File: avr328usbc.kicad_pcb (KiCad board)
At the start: 2 copper layers, 21 parts, among them J1 USB_C_Receptacle, J2 Conn_02x05_Counter_Clockwise, J3 USB_C_Receptacle_PowerOnly_6P, J4 Conn_02x16_Counter_Clockwise, J5 AVR-ISP-6, U1 MCP2221AxP, U2 ACPL-772L-000E, U3 ACPL-772L-000E, U4 ATmega328P-P

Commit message: finished converting schematic to correct USBC and pin headers
Symbols didn't match the footprints
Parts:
- J1: value USB_C_Receptacle -> USB-C THT
- J2: value Conn_02x05_Counter_Clockwise -> MCP Debug Header
- J3: value USB_C_Receptacle_PowerOnly_6P -> USB-C THT
- J4: value Conn_02x16_Counter_Clockwise -> AVR Pin Header
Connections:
- J2 pad 10: GND_USB -> /MCP.SDA
- J2 pad 2: /MCP.GP0 -> GND_USB
- J2 pad 3: /MCP.GP1 -> /MCP.GP0
- J2 pad 4: /MCP.GP2 -> /MCP.UTx
- J2 pad 5: /MCP.GP3 -> /MCP.GP1
- J2 pad 6: /MCP.SDA -> /MCP.URx
- J2 pad 7: /MCP.SCL -> /MCP.GP2
- J2 pad 8: /MCP.URx -> /MCP.SCL
- J2 pad 9: /MCP.UTx -> /MCP.GP3
- J3 pad A1: (no net) -> GND_AVR
- J3 pad A4: (no net) -> VCC_AVR
- J3 pad A6: (no net) -> unconnected-(J3-D+-PadA6)
- J3 pad A7: (no net) -> unconnected-(J3-D--PadA7)
- J3 pad A8: (no net) -> unconnected-(J3-SBU1-PadA8)
- J3 pad B1: (no net) -> GND_AVR
- J3 pad B4: (no net) -> VCC_AVR
- J3 pad B6: (no net) -> unconnected-(J3-D+-PadB6)
- J3 pad B7: (no net) -> unconnected-(J3-D--PadB7)
- J3 pad B8: (no net) -> unconnected-(J3-SBU2-PadB8)
- J4 pad 10: /MCU Sheet/PC1 -> /MCU Sheet/PD4
- J4 pad 11: /MCU Sheet/PC2 -> /MCU Sheet/PB5
- J4 pad 12: /MCU Sheet/PC3 -> /MCU Sheet/PD5
- J4 pad 13: /MCU Sheet/PC4 -> /MCU Sheet/PB6
- J4 pad 14: /MCU Sheet/PC5 -> /MCU Sheet/PD6
- J4 pad 15: /MCU Sheet/PC6 #RESET -> /MCU Sheet/PB7
- J4 pad 16: GND_AVR -> /MCU Sheet/PD7
- J4 pad 17: VCC_AVR -> /MCU Sheet/PC0
- J4 pad 18: unconnected-(J4-Pin_18-Pad18) -> GND_AVR
- J4 pad 19: unconnected-(J4-Pin_19-Pad19) -> /MCU Sheet/PC1
- J4 pad 2: /MCU Sheet/PB1 -> /UART_Rx
- J4 pad 21: unconnected-(J4-Pin_21-Pad21) -> /MCU Sheet/PC2
- J4 pad 23: unconnected-(J4-Pin_23-Pad23) -> /MCU Sheet/PC3
- J4 pad 24: GND_AVR -> unconnected-(J4-Pin_24-Pad24)
- J4 pad 25: /MCU Sheet/PD7 -> /MCU Sheet/PC4
- J4 pad 26: /MCU Sheet/PD6 -> unconnected-(J4-Pin_26-Pad26)
- J4 pad 27: /MCU Sheet/PD5 -> /MCU Sheet/PC5
- J4 pad 28: /MCU Sheet/PD4 -> unconnected-(J4-Pin_28-Pad28)
- J4 pad 29: /MCU Sheet/PD3 -> /MCU Sheet/PC6 #RESET
- J4 pad 3: /MCU Sheet/PB2 -> /MCU Sheet/PB1
- J4 pad 30: /MCU Sheet/PD2 -> unconnected-(J4-Pin_30-Pad30)
- J4 pad 31: /UART_Tx -> GND_AVR
- J4 pad 32: /UART_Rx -> VCC_AVR
- J4 pad 4: /MCU Sheet/PB3 -> /UART_Tx
- J4 pad 5: /MCU Sheet/PB4 -> /MCU Sheet/PB2
- J4 pad 6: /MCU Sheet/PB5 -> /MCU Sheet/PD2
- J4 pad 7: /MCU Sheet/PB6 -> /MCU Sheet/PB3
- J4 pad 8: /MCU Sheet/PB7 -> /MCU Sheet/PD3
- J4 pad 9: /MCU Sheet/PC0 -> /MCU Sheet/PB4

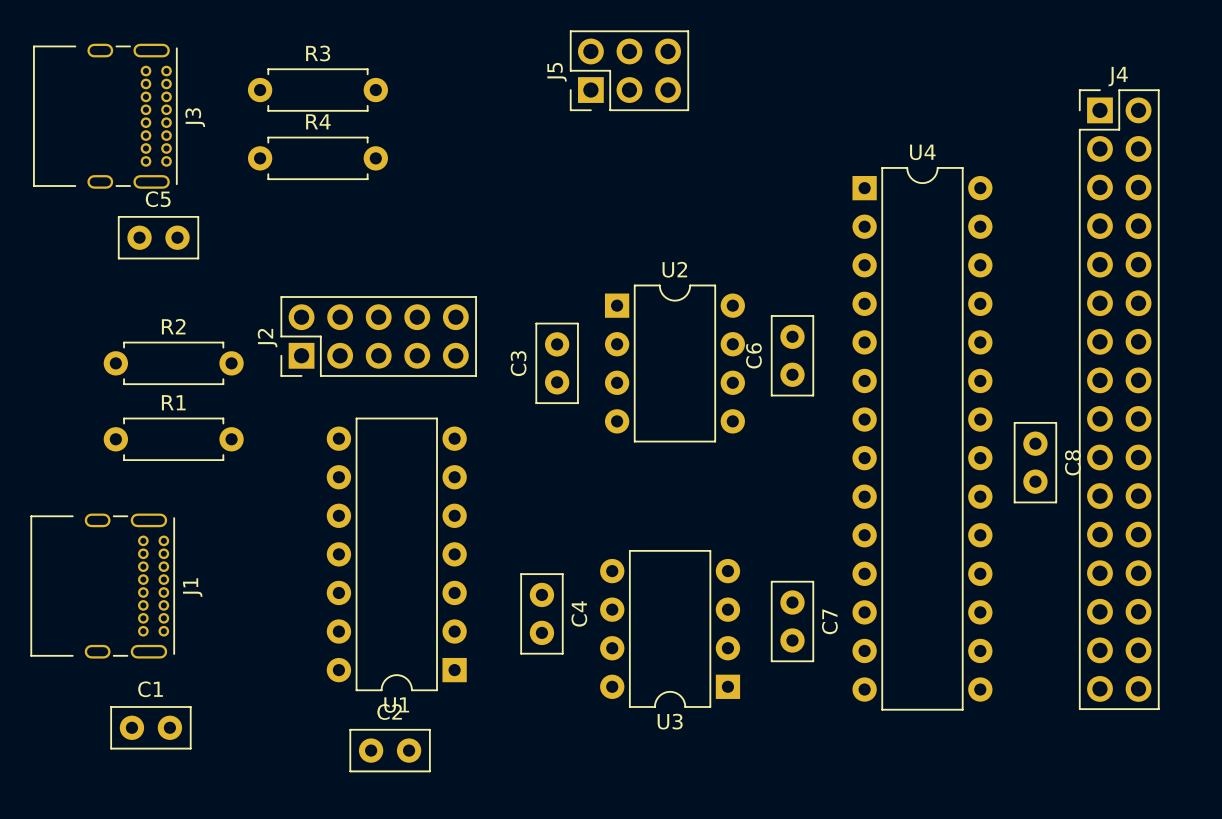
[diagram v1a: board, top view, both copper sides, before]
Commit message: pcb footprints placed and locked
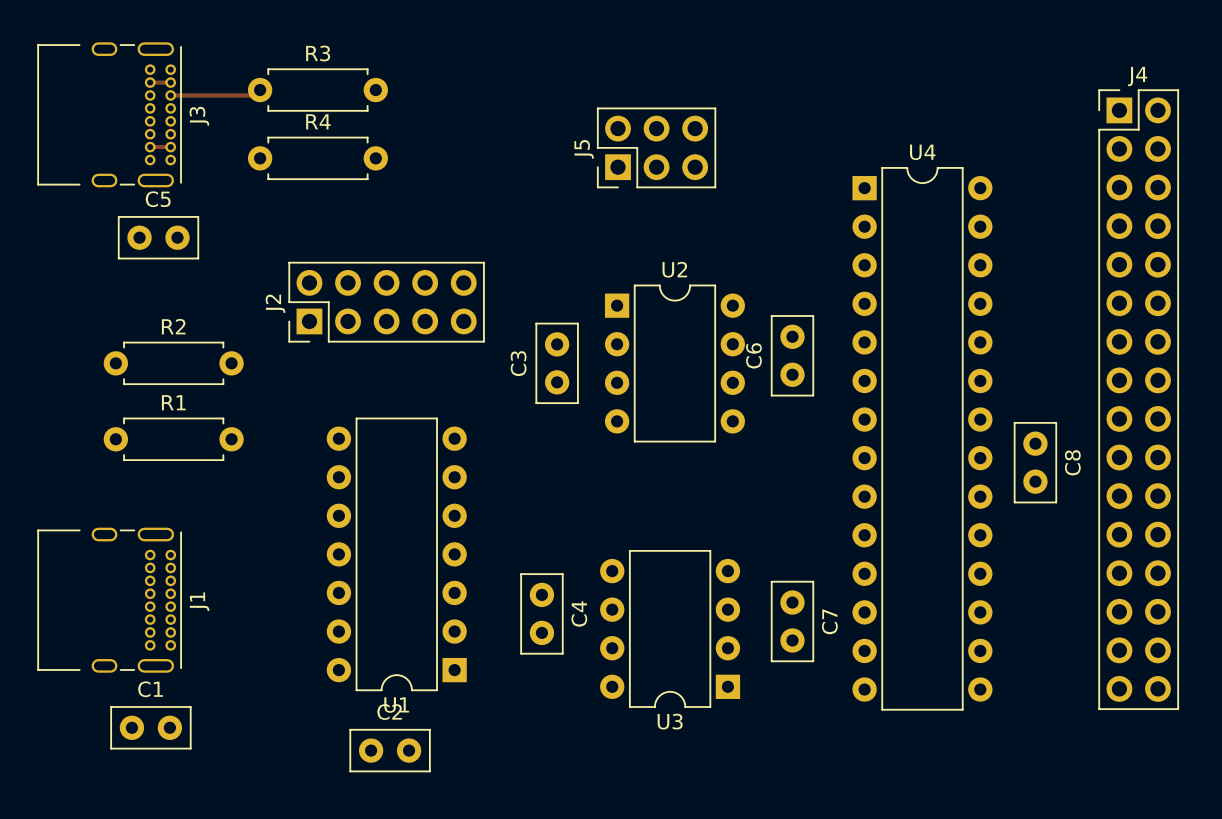
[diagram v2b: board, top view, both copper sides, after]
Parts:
- moved J5 5.38 mm to (111.8, 68.6)
- moved J2 2.32 mm to (91.4, 78.7)
- moved J4 1.28 mm to (144.8, 64.8)
- moved J1 1.04 mm to (82.3, 94.1)
- moved J3 0.29 mm to (82.3, 62.2)
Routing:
- net Net-(J3-CC1): track 0.00 -> 6.04 mm
- net VCC_AVR: track 0.00 -> 2.70 mm
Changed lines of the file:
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@@
 	(generator_version "8.0")
 	(general
-		(thickness 1.6)
+		(thickness 1.6002)
 		(legacy_teardrops no)
 	)
@@
 	)
 	(setup
+		(stackup
+			(layer "F.SilkS"
+				(type "Top Silk Screen")
+			)
+			(layer "F.Paste"
+				(type "Top Solder Paste")
+			)
+			(layer "F.Mask"
+				(type "Top Solder Mask")
+				(thickness 0.0254)
+			)
+			(layer "F.Cu"
+				(type "copper")
+				(thickness 0.03556)
+			)
+			(layer "dielectric 1"
+				(type "core")
+				(thickness 1.47828)
+				(material "FR4")
+				(epsilon_r 4.5)
+				(loss_tangent 0.02)
+			)
+			(layer "B.Cu"
+				(type "copper")
+				(thickness 0.03556)
+			)
+			(layer "B.Mask"
+				(type "Bottom Solder Mask")
+				(thickness 0.0254)
+			)
+			(layer "B.Paste"
+				(type "Bottom Solder Paste")
+			)
+			(layer "B.SilkS"
+				(type "Bottom Silk Screen")
+			)
+			(copper_finish "None")
+			(dielectric_constraints no)
+		)
 		(pad_to_mask_clearance 0)
 		(allow_soldermask_bridges_in_footprints no)
@@
 	(net 61 "unconnected-(J4-Pin_24-Pad24)")
 	(footprint "Package_DIP:DIP-8_W7.62mm"
+		(locked yes)
 		(layer "F.Cu")
 		(at 119 102.8 180)
@@
 	)
 	(footprint "Resistor_THT:R_Axial_DIN0207_L6.3mm_D2.5mm_P7.62mm_Horizontal"
+		(locked yes)
 		(layer "F.Cu")
 		(at 88.19 63.5)
@@
 	)
 	(footprint "Package_DIP:DIP-14_W7.62mm"
+		(locked yes)
 		(layer "F.Cu")
 		(at 101 101.7 180)
@@
 	)
 	(footprint "Connector_USB:USB_C_Receptacle_GCT_USB4085"
+		(locked yes)
 		(layer "F.Cu")
-		(at 82.025 62.25 -90)
+		(at 82.301145 62.157471 -90)
 		(descr "USB 2.0 Type C Receptacle, https://gct.co/Files/Drawings/USB4085.pdf")
 		(tags "USB Type-C Receptacle Through-hole Right angle")
@@
 	)
 	(footprint "Resistor_THT:R_Axial_DIN0207_L6.3mm_D2.5mm_P7.62mm_Horizontal"
+		(locked yes)
 		(layer "F.Cu")
 		(at 88.19 68)
@@
 	)
 	(footprint "Capacitor_THT:C_Disc_D5.0mm_W2.5mm_P2.50mm"
+		(locked yes)
 		(layer "F.Cu")
 		(at 123.25 82.25 90)
@@
 	)
 	(footprint "Connector_PinHeader_2.54mm:PinHeader_2x16_P2.54mm_Vertical"
+		(locked yes)
 		(layer "F.Cu")
-		(at 143.5 64.84)
+		(at 144.78 64.84)
 		(descr "Through hole straight pin header, 2x16, 2.54mm pitch, double rows")
 		(tags "Through hole pin header THT 2x16 2.54mm double row")
@@
 	)
 	(footprint "Capacitor_THT:C_Disc_D5.0mm_W2.5mm_P2.50mm"
+		(locked yes)
 		(layer "F.Cu")
 		(at 79.75 105.5)
@@
 	)
 	(footprint "Resistor_THT:R_Axial_DIN0207_L6.3mm_D2.5mm_P7.62mm_Horizontal"
+		(locked yes)
 		(layer "F.Cu")
 		(at 78.69 81.5)
@@
 	)
 	(footprint "Package_DIP:DIP-8_W7.62mm"
+		(locked yes)
 		(layer "F.Cu")
 		(at 111.7 77.7)
@@
 	)
 	(footprint "Capacitor_THT:C_Disc_D5.0mm_W2.5mm_P2.50mm"
+		(locked yes)
 		(layer "F.Cu")
 		(at 123.25 97.25 -90)
@@
 	)
 	(footprint "Connector_USB:USB_C_Receptacle_GCT_USB4085"
+		(locked yes)
 		(layer "F.Cu")
-		(at 81.85 93.19 -90)
+		(at 82.303596 94.121754 -90)
 		(descr "USB 2.0 Type C Receptacle, https://gct.co/Files/Drawings/USB4085.pdf")
 		(tags "USB Type-C Receptacle Through-hole Right angle")
@@
 	)
 	(footprint "Connector_PinHeader_2.54mm:PinHeader_2x03_P2.54mm_Vertical"
+		(locked yes)
 		(layer "F.Cu")
-		(at 109.975 63.5 90)
+		(at 111.76 68.58 90)
 		(descr "Through hole straight pin header, 2x03, 2.54mm pitch, double rows")
 		(tags "Through hole pin header THT 2x03 2.54mm double row")
@@
 	)
 	(footprint "Capacitor_THT:C_Disc_D5.0mm_W2.5mm_P2.50mm"
+		(locked yes)
 		(layer "F.Cu")
 		(at 95.5 107)
@@
 	)
 	(footprint "Capacitor_THT:C_Disc_D5.0mm_W2.5mm_P2.50mm"
+		(locked yes)
 		(layer "F.Cu")
 		(at 107.75 82.75 90)
@@
 	)
 	(footprint "Resistor_THT:R_Axial_DIN0207_L6.3mm_D2.5mm_P7.62mm_Horizontal"
+		(locked yes)
 		(layer "F.Cu")
 		(at 78.69 86.5)
@@
 	)
 	(footprint "Capacitor_THT:C_Disc_D5.0mm_W2.5mm_P2.50mm"
+		(locked yes)
 		(layer "F.Cu")
 		(at 139.25 86.79 -90)
@@
 	)
 	(footprint "Package_DIP:DIP-28_W7.62mm"
+		(locked yes)
 		(layer "F.Cu")
 		(at 128 69.96)
@@
 	)
 	(footprint "Capacitor_THT:C_Disc_D5.0mm_W2.5mm_P2.50mm"
+		(locked yes)
 		(layer "F.Cu")
 		(at 80.25 73.225)
@@
 	)
 	(footprint "Capacitor_THT:C_Disc_D5.0mm_W2.5mm_P2.50mm"
+		(locked yes)
 		(layer "F.Cu")
 		(at 106.75 96.75 -90)
@@
 	)
 	(footprint "Connector_PinHeader_2.54mm:PinHeader_2x05_P2.54mm_Vertical"
+		(locked yes)
 		(layer "F.Cu")
-		(at 90.92 81 90)
+		(at 91.44 78.74 90)
 		(descr "Through hole straight pin header, 2x05, 2.54mm pitch, double rows")
 		(tags "Through hole pin header THT 2x05 2.54mm double row")
@@
 		)
 	)
+	(gr_line
+		(start 76.2 50.8)
+		(end 76.2 111.76)
+		(locked yes)
+		(stroke
+			(width 0.1)
+			(type default)
+		)
+		(layer "Dwgs.User")
+	)
+	(segment
+		(start 80.951145 67.257471)
+		(end 82.301145 67.257471)
+		(width 0.254)
+		(layer "F.Cu")
+		(net 4)
+	)
+	(segment
+		(start 80.951145 63.007471)
+		(end 82.301145 63.007471)
+		(width 0.254)
+		(layer "F.Cu")
+		(net 4)
+	)
+	(segment
+		(start 82.301145 63.857471)
+		(end 87.832529 63.857471)
+		(width 0.254)
+		(layer "F.Cu")
+		(net 47)
+	)
+	(segment
+		(start 87.832529 63.857471)
+		(end 88.19 63.5)
+		(width 0.254)
+		(layer "F.Cu")
+		(net 47)
+	)
 )

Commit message: routed most non-header signals
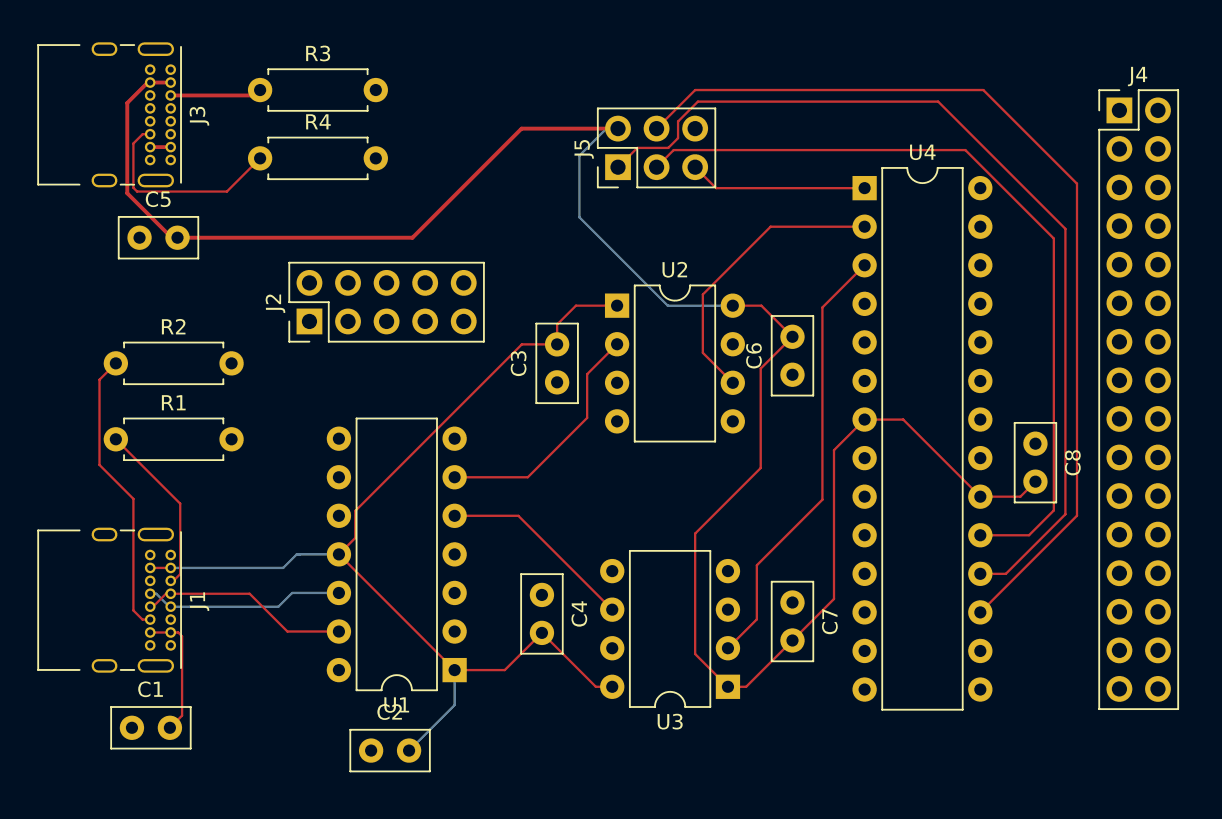
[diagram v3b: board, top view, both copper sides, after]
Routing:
- net VCC_AVR: track 2.70 -> 134.2 mm
- net VCC_USB: track 0.00 -> 78.5 mm
- net /MCU Sheet/PB3: track 0.00 -> 62.2 mm
- net /MCU Sheet/PB4: track 0.00 -> 61.4 mm
- net /MCU Sheet/PB5: track 0.00 -> 52.5 mm
- net /UART_Tx: track 0.00 -> 28.9 mm
- net /UART_Rx: track 0.00 -> 19.1 mm
- net Net-(J1-CC2): track 0.00 -> 19.0 mm
- net /MCP.UTx: track 0.00 -> 16.0 mm
- net /D+: track 0.00 -> 13.8 mm
- net Net-(J3-CC2): track 0.00 -> 13.6 mm
- net /D-: track 0.00 -> 13.2 mm
- net /MCP.URx: track 0.00 -> 12.9 mm
- net /MCU Sheet/PC6 #RESET: track 0.00 -> 11.7 mm
- net Net-(J1-CC1): track 0.00 -> 11.4 mm

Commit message: reordered pins and routed MCP header
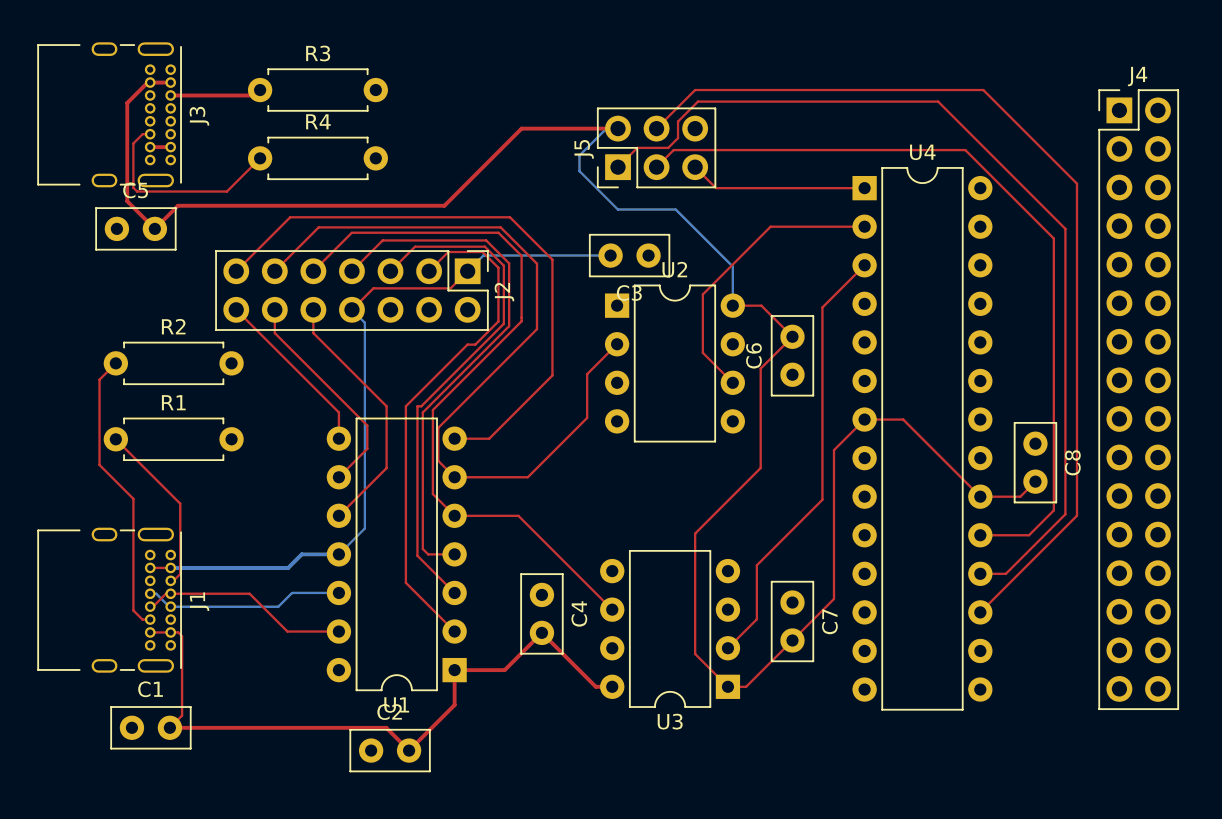
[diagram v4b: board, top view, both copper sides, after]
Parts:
- J2: footprint Connector_PinHeader_2.54mm:PinHeader_2x05_P2.54mm_Vertical -> Connector_PinHeader_2.54mm:PinHeader_2x07_P2.54mm_Vertical
- moved J2 10.9 mm to (101.9, 75.4), turned to -90 degrees
- moved C3 10.3 mm to (113.8, 74.4), turned to 180 degrees
- moved C5 1.60 mm to (78.8, 72.6)
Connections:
- J2 pad 1: /MCP.#RST -> VCC_USB
- J2 pad 10: /MCP.SDA -> /MCP.SCL
- J2 pad 4: /MCP.UTx -> unconnected-(J2-Pin_4-Pad4)
- J2 pad 6: /MCP.URx -> unconnected-(J2-Pin_6-Pad6)
- J2 pad 7: /MCP.GP2 -> /MCP.#RST
- J2 pad 8: /MCP.SCL -> VCC_USB
- J2 pad 9: /MCP.GP3 -> /MCP.URx
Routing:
- net /MCP.GP2: track 0.00 -> 39.2 mm
- net /MCP.UTx: track 16.0 -> 52.7 mm
- net /MCP.URx: track 12.9 -> 48.5 mm
- net /MCP.#RST: track 0.00 -> 35.2 mm
- net /MCP.GP1: track 0.00 -> 33.7 mm
- net /MCP.GP0: track 0.00 -> 33.6 mm
- net /MCP.SCL: track 0.00 -> 17.1 mm
- net VCC_USB: track 78.5 -> 92.8 mm
- net /MCP.SDA: track 0.00 -> 14.3 mm
- net /MCP.GP3: track 0.00 -> 11.3 mm

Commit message: changed MCP header into two headers mirroring part
also rearanged components on board
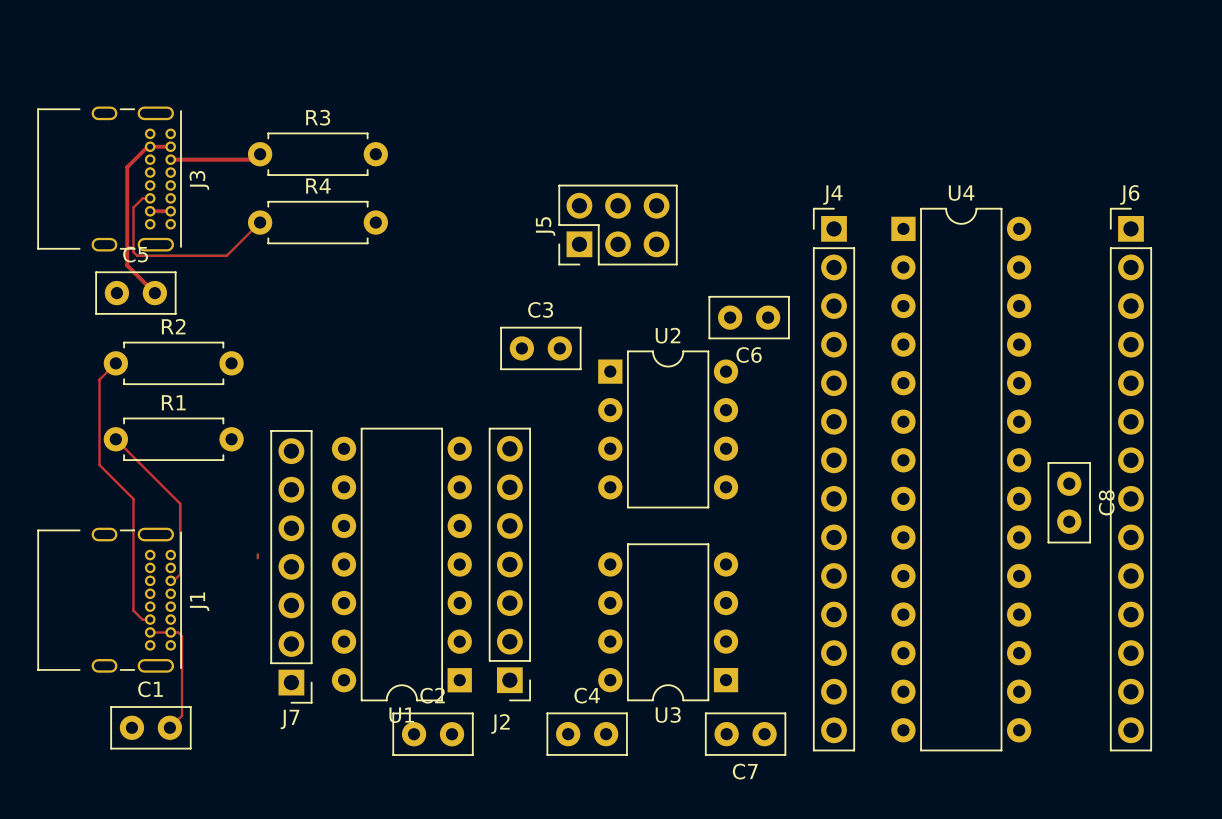
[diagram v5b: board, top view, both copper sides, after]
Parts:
- added J6: Conn_01x14_MountingPin, Connector_PinHeader_2.54mm:PinHeader_1x14_P2.54mm_Vertical, F.Cu at (145.5, 72.6)
- added J7: MCP Debug Header, Connector_PinHeader_2.54mm:PinHeader_1x07_P2.54mm_Vertical, F.Cu at (90.3, 102.5)
- J2: footprint Connector_PinHeader_2.54mm:PinHeader_2x07_P2.54mm_Vertical -> Connector_PinHeader_2.54mm:PinHeader_1x07_P2.54mm_Vertical
- J4: value AVR Pin Header -> Conn_01x14_MountingPin; footprint Connector_PinHeader_2.54mm:PinHeader_2x16_P2.54mm_Vertical -> Connector_PinHeader_2.54mm:PinHeader_1x14_P2.54mm_Vertical
- moved J2 27.1 mm to (104.6, 102.4), turned to 180 degrees
- moved J4 20.4 mm to (126.0, 72.6)
- moved C3 10.3 mm to (105.4, 80.5), turned to 0 degrees
- moved C4 9.33 mm to (108.5, 105.9), turned to 0 degrees
- moved C7 8.86 mm to (121.4, 105.9), turned to 180 degrees
- moved J5 5.68 mm to (109.2, 73.7)
- moved U2 4.37 mm to (111.3, 82.0)
- moved J3 4.23 mm to (82.3, 66.4)
- moved R3 4.23 mm to (88.2, 67.7)
- moved R4 4.23 mm to (88.2, 72.2)
- moved C5 4.23 mm to (78.8, 76.9)
- moved C6 4.09 mm to (121.6, 78.5), turned to 180 degrees
- moved U4 3.71 mm to (130.6, 72.6)
- moved C8 3.45 mm to (141.5, 89.4)
- moved C2 3.03 mm to (98.3, 105.9)
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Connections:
- J2 pad 2: GND_USB -> /MCP.GP0
- J2 pad 3: /MCP.GP0 -> /MCP.GP1
- J2 pad 4: unconnected-(J2-Pin_4-Pad4) -> /MCP.#RST
- J2 pad 5: /MCP.GP1 -> /MCP.URx
- J2 pad 6: unconnected-(J2-Pin_6-Pad6) -> /MCP.UTx
- J2 pad 7: /MCP.#RST -> /MCP.GP2
- J4 pad 1: /MCU Sheet/PB0 -> /MCU Sheet/PC6 #RESET
- J4 pad 10: /MCU Sheet/PD4 -> /MCU Sheet/PB7
- J4 pad 11: /MCU Sheet/PB5 -> /MCU Sheet/PD5
- J4 pad 12: /MCU Sheet/PD5 -> /MCU Sheet/PD6
- J4 pad 13: /MCU Sheet/PB6 -> /MCU Sheet/PD7
- J4 pad 14: /MCU Sheet/PD6 -> /MCU Sheet/PB0
- J4 pad 3: /MCU Sheet/PB1 -> /UART_Tx
- J4 pad 4: /UART_Tx -> /MCU Sheet/PD2
- J4 pad 5: /MCU Sheet/PB2 -> /MCU Sheet/PD3
- J4 pad 6: /MCU Sheet/PD2 -> /MCU Sheet/PD4
- J4 pad 7: /MCU Sheet/PB3 -> VCC_AVR
- J4 pad 8: /MCU Sheet/PD3 -> GND_AVR
- J4 pad 9: /MCU Sheet/PB4 -> /MCU Sheet/PB6
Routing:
- net VCC_AVR: track 133.8 -> 13.8 mm
- net VCC_USB: track 92.8 -> 8.56 mm
- net /MCU Sheet/PB3: track 62.2 -> 0.00 mm
- net /MCU Sheet/PB4: track 61.4 -> 0.00 mm
- net /MCP.UTx: track 52.7 -> 0.00 mm
- net /MCU Sheet/PB5: track 52.5 -> 0.00 mm
- net /MCP.URx: track 48.5 -> 0.00 mm
- net /MCP.GP2: track 39.2 -> 0.00 mm
- net /MCP.#RST: track 35.2 -> 0.00 mm
- net /MCP.GP1: track 33.7 -> 0.00 mm
- net /MCP.GP0: track 33.6 -> 0.00 mm
- net /UART_Tx: track 28.9 -> 0.00 mm
- net /UART_Rx: track 19.1 -> 0.00 mm
- net /MCP.SCL: track 17.1 -> 0.26 mm
- net /MCP.SDA: track 14.3 -> 0.00 mm
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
